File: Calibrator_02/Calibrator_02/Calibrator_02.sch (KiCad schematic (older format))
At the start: 22 parts, among them J1 Conn_01x04, J2 DB9_Female_MountingHoles, J3 Conn_Coaxial, J4 Conn_01x01_Female, J5 Conn_01x01_Female, J6 Conn_01x04, M1 AW9523BTQR, U1 KAQY214STLD, U2 KAQY214STLD, U3 KAQY214STLD, U4 KAQY214STLD, U5 KAQY214STLD, U6 KAQY214STLD, U7 KAQY214STLD, U8 KAQY214STLD

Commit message: Added Resistors to Diodes
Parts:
- added R10, R17: 95.3 1%, Resistor_SMD:R_0201_0603Metric_Pad0.64x0.40mm_HandSolder, symbol Device:R
- added R11, R12, R13, R14, R15, R16: 84.5 1%, Resistor_SMD:R_0201_0603Metric_Pad0.64x0.40mm_HandSolder, symbol Device:R
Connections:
- net +3V3: now also R10.1, R11.1, R12.1, R13.1, R14.2, R15.2, R16.2, R17.2; no longer D1.2 (A), D2.2 (A), U1.1 (A), U2.1 (A), U4.1 (A), U5.1 (A), U7.1 (A), U8.1 (A)
- new net: R13.2, U4.1 (A)
- new net: R15.1, U7.1 (A)
- new net: D1.2 (A), R10.2
- new net: D2.2 (A), R17.1
- new net: R14.1, U5.1 (A)
- new net: R12.2, U2.1 (A)
- new net: R16.1, U8.1 (A)
- new net: R11.2, U1.1 (A)
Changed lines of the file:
@@
 Wire Wire Line
 	2150 6600 2750 6600
-Wire Wire Line
-	7900 700  6550 700
-Connection ~ 6550 700
-Wire Wire Line
-	1700 700  3700 700
-Connection ~ 5100 700
-Wire Wire Line
-	5100 700  6550 700
-Connection ~ 3700 700
-Wire Wire Line
-	3700 700  5100 700
 $Comp
 L power:+3.3V #PWR01
@@
 	-1   0    0    1
 $EndComp
-Connection ~ 4500 5500
-Wire Wire Line
-	4500 5500 5950 5500
-Connection ~ 5950 5500
-Wire Wire Line
-	5950 5500 7300 5500
 $Comp
 L Connector_Generic:Conn_01x04 J1
@@
 	1    0    0    -1
 $EndComp
-Wire Wire Line
-	7300 4750 7300 5500
-Wire Wire Line
-	5950 4850 5950 5500
-Wire Wire Line
-	4500 4800 4500 5500
-Wire Wire Line
-	2100 5500 3100 5500
-Wire Wire Line
-	3100 5100 3100 5500
-Connection ~ 3100 5500
-Wire Wire Line
-	3100 5500 4500 5500
-Wire Wire Line
-	7900 700  7900 1500
-Wire Wire Line
-	6550 700  6550 1600
-Wire Wire Line
-	5100 700  5100 1700
-Wire Wire Line
-	3700 700  3700 1350
 $Comp
 L Connector:Conn_Coaxial J?
@@
 	-1   0    0    1
 $EndComp
+Wire Wire Line
+	2100 5500 3100 5500
+Wire Wire Line
+	1700 700  3700 700
+$Comp
+L Device:R R10
+U 1 1 6283AB55
+P 3700 1200
+F 0 "R10" H 3770 1246 50  0000 L CNN
+F 1 "95.3 1%" H 3770 1155 50  0000 L CNN
+F 2 "Resistor_SMD:R_0201_0603Metric_Pad0.64x0.40mm_HandSolder" V 3630 1200 50  0001 C CNN
+F 3 "~" H 3700 1200 50  0001 C CNN
+F 4 "C218188" H 3700 1200 50  0001 C CNN "LCSC"
+	1    3700 1200
+	1    0    0    -1
+$EndComp
+$Comp
+L Device:R R13
+U 1 1 6283B6FF
+P 5100 1550
+F 0 "R13" H 5170 1596 50  0000 L CNN
+F 1 "84.5 1%" H 5170 1505 50  0000 L CNN
+F 2 "Resistor_SMD:R_0201_0603Metric_Pad0.64x0.40mm_HandSolder" V 5030 1550 50  0001 C CNN
+F 3 "~" H 5100 1550 50  0001 C CNN
+F 4 "C177824" H 5100 1550 50  0001 C CNN "LCSC"
+	1    5100 1550
+	1    0    0    -1
+$EndComp
+$Comp
+L Device:R R17
+U 1 1 6283E3B1
+P 3100 5250
+F 0 "R17" H 3170 5296 50  0000 L CNN
+F 1 "95.3 1%" H 3170 5205 50  0000 L CNN
+F 2 "Resistor_SMD:R_0201_0603Metric_Pad0.64x0.40mm_HandSolder" V 3030 5250 50  0001 C CNN
+F 3 "~" H 3100 5250 50  0001 C CNN
+F 4 "C218188" H 3100 5250 50  0001 C CNN "LCSC"
+	1    3100 5250
+	1    0    0    -1
+$EndComp
+$Comp
+L Device:R R12
+U 1 1 6287964B
+P 6550 1450
+F 0 "R12" H 6620 1496 50  0000 L CNN
+F 1 "84.5 1%" H 6620 1405 50  0000 L CNN
+F 2 "Resistor_SMD:R_0201_0603Metric_Pad0.64x0.40mm_HandSolder" V 6480 1450 50  0001 C CNN
+F 3 "~" H 6550 1450 50  0001 C CNN
+F 4 "C177824" H 6550 1450 50  0001 C CNN "LCSC"
+	1    6550 1450
+	1    0    0    -1
+$EndComp
+$Comp
+L Device:R R11
+U 1 1 6287B511
+P 7900 1350
+F 0 "R11" H 7970 1396 50  0000 L CNN
+F 1 "84.5 1%" H 7970 1305 50  0000 L CNN
+F 2 "Resistor_SMD:R_0201_0603Metric_Pad0.64x0.40mm_HandSolder" V 7830 1350 50  0001 C CNN
+F 3 "~" H 7900 1350 50  0001 C CNN
+F 4 "C177824" H 7900 1350 50  0001 C CNN "LCSC"
+	1    7900 1350
+	1    0    0    -1
+$EndComp
+$Comp
+L Device:R R15
+U 1 1 6287D697
+P 4500 4950
+F 0 "R15" H 4570 4996 50  0000 L CNN
+F 1 "84.5 1%" H 4570 4905 50  0000 L CNN
+F 2 "Resistor_SMD:R_0201_0603Metric_Pad0.64x0.40mm_HandSolder" V 4430 4950 50  0001 C CNN
+F 3 "~" H 4500 4950 50  0001 C CNN
+F 4 "C177824" H 4500 4950 50  0001 C CNN "LCSC"
+	1    4500 4950
+	1    0    0    -1
+$EndComp
+$Comp
+L Device:R R16
+U 1 1 6287F5DB
+P 5950 5000
+F 0 "R16" H 6020 5046 50  0000 L CNN
+F 1 "84.5 1%" H 6020 4955 50  0000 L CNN
+F 2 "Resistor_SMD:R_0201_0603Metric_Pad0.64x0.40mm_HandSolder" V 5880 5000 50  0001 C CNN
+F 3 "~" H 5950 5000 50  0001 C CNN
+F 4 "C177824" H 5950 5000 50  0001 C CNN "LCSC"
+	1    5950 5000
+	1    0    0    -1
+$EndComp
+$Comp
+L Device:R R14
+U 1 1 628831ED
+P 7300 4900
+F 0 "R14" H 7370 4946 50  0000 L CNN
+F 1 "84.5 1%" H 7370 4855 50  0000 L CNN
+F 2 "Resistor_SMD:R_0201_0603Metric_Pad0.64x0.40mm_HandSolder" V 7230 4900 50  0001 C CNN
+F 3 "~" H 7300 4900 50  0001 C CNN
+F 4 "C177824" H 7300 4900 50  0001 C CNN "LCSC"
+	1    7300 4900
+	1    0    0    -1
+$EndComp
+Wire Wire Line
+	7300 5050 7300 5500
+Wire Wire Line
+	5950 5150 5950 5500
+Connection ~ 5950 5500
+Wire Wire Line
+	5950 5500 7300 5500
+Wire Wire Line
+	4500 5100 4500 5500
+Connection ~ 4500 5500
+Wire Wire Line
+	4500 5500 5950 5500
+Wire Wire Line
+	3100 5400 3100 5500
+Connection ~ 3100 5500
+Wire Wire Line
+	3100 5500 4500 5500
+Connection ~ 3700 700
+Wire Wire Line
+	3700 700  5100 700
+Wire Wire Line
+	5100 700  5100 1400
+Connection ~ 5100 700
+Wire Wire Line
+	5100 700  6550 700
+Wire Wire Line
+	6550 700  6550 1300
+Connection ~ 6550 700
+Wire Wire Line
+	6550 700  7900 700
+Wire Wire Line
+	7900 1200 7900 700
+Wire Wire Line
+	3700 700  3700 1050
 $EndSCHEMATC

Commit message: Update
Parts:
- removed JP1: Jumper, Jumper:SolderJumper-2_P1.3mm_Open_RoundedPad1.0x1.5mm, symbol Device:Jumper
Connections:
- net +3V3: now also J4.1 (Pin_1), M1.23 (RSTN)
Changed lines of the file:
@@
 Wire Wire Line
 	9050 2900 9350 2900
-Wire Wire Line
-	1700 6500 1800 6500
-$Comp
-L Device:Jumper JP1
-U 1 1 627E9ED5
-P 1800 6200
-F 0 "JP1" V 1754 6327 50  0000 L CNN
-F 1 "Jumper" V 1845 6327 50  0000 L CNN
-F 2 "Jumper:SolderJumper-2_P1.3mm_Open_RoundedPad1.0x1.5mm" H 1800 6200 50  0001 C CNN
-F 3 "~" H 1800 6200 50  0001 C CNN
-	1    1800 6200
-	0    1    1    0
-$EndComp
-Connection ~ 1800 6500
-Wire Wire Line
-	1800 6500 2750 6500
 $Comp
 L power:+3.3V #PWR09
@@
 Wire Wire Line
 	3700 700  3700 1050
+Wire Wire Line
+	1700 6500 1800 6500
+Wire Wire Line
+	1800 5900 1800 6500
+Connection ~ 1800 6500
+Wire Wire Line
+	1800 6500 2750 6500
 $EndSCHEMATC

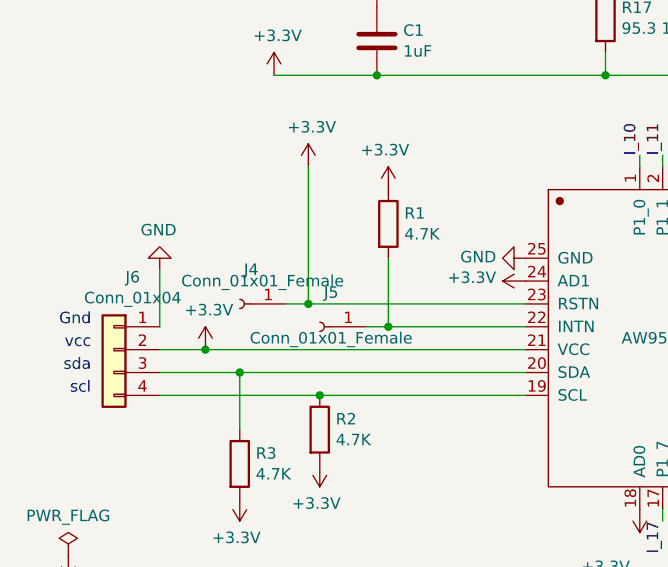
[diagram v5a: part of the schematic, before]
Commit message: Fixed footprint
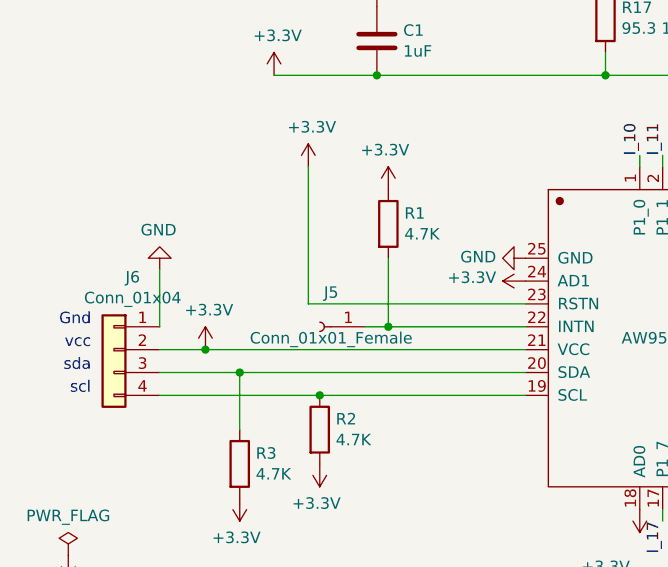
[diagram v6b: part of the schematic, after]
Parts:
- removed J4: Conn_01x01_Female, Connector_PinSocket_2.54mm:PinSocket_1x01_P2.54mm_Horizontal, symbol Connector:Conn_01x01_Female
- R10, R11, R12, R13, R14, R15, R16, R17: footprint Resistor_SMD:R_0201_0603Metric_Pad0.64x0.40mm_HandSolder -> Resistor_SMD:R_0603_1608Metric_Pad0.98x0.95mm_HandSolder
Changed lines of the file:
@@
-$EndComp
-$Comp
-L Connector:Conn_01x01_Female J4
-U 1 1 6281DACE
-P 1500 6500
-F 0 "J4" H 1450 6650 50  0000 C CNN
-F 1 "Conn_01x01_Female" H 1400 6600 50  0000 C CNN
-F 2 "Connector_PinSocket_2.54mm:PinSocket_1x01_P2.54mm_Horizontal" H 1500 6500 50  0001 C CNN
-F 3 "~" H 1500 6500 50  0001 C CNN
-	1    1500 6500
-	-1   0    0    -1
 $EndComp
 $Comp
@@
 F 0 "R10" H 3770 1246 50  0000 L CNN
 F 1 "95.3 1%" H 3770 1155 50  0000 L CNN
-F 2 "Resistor_SMD:R_0201_0603Metric_Pad0.64x0.40mm_HandSolder" V 3630 1200 50  0001 C CNN
+F 2 "Resistor_SMD:R_0603_1608Metric_Pad0.98x0.95mm_HandSolder" V 3630 1200 50  0001 C CNN
 F 3 "~" H 3700 1200 50  0001 C CNN
 F 4 "C218188" H 3700 1200 50  0001 C CNN "LCSC"
@@
 F 0 "R13" H 5170 1596 50  0000 L CNN
 F 1 "84.5 1%" H 5170 1505 50  0000 L CNN
-F 2 "Resistor_SMD:R_0201_0603Metric_Pad0.64x0.40mm_HandSolder" V 5030 1550 50  0001 C CNN
+F 2 "Resistor_SMD:R_0603_1608Metric_Pad0.98x0.95mm_HandSolder" V 5030 1550 50  0001 C CNN
 F 3 "~" H 5100 1550 50  0001 C CNN
 F 4 "C177824" H 5100 1550 50  0001 C CNN "LCSC"
@@
 F 0 "R17" H 3170 5296 50  0000 L CNN
 F 1 "95.3 1%" H 3170 5205 50  0000 L CNN
-F 2 "Resistor_SMD:R_0201_0603Metric_Pad0.64x0.40mm_HandSolder" V 3030 5250 50  0001 C CNN
+F 2 "Resistor_SMD:R_0603_1608Metric_Pad0.98x0.95mm_HandSolder" V 3030 5250 50  0001 C CNN
 F 3 "~" H 3100 5250 50  0001 C CNN
 F 4 "C218188" H 3100 5250 50  0001 C CNN "LCSC"
@@
 F 0 "R12" H 6620 1496 50  0000 L CNN
 F 1 "84.5 1%" H 6620 1405 50  0000 L CNN
-F 2 "Resistor_SMD:R_0201_0603Metric_Pad0.64x0.40mm_HandSolder" V 6480 1450 50  0001 C CNN
+F 2 "Resistor_SMD:R_0603_1608Metric_Pad0.98x0.95mm_HandSolder" V 6480 1450 50  0001 C CNN
 F 3 "~" H 6550 1450 50  0001 C CNN
 F 4 "C177824" H 6550 1450 50  0001 C CNN "LCSC"
@@
 F 0 "R11" H 7970 1396 50  0000 L CNN
 F 1 "84.5 1%" H 7970 1305 50  0000 L CNN
-F 2 "Resistor_SMD:R_0201_0603Metric_Pad0.64x0.40mm_HandSolder" V 7830 1350 50  0001 C CNN
+F 2 "Resistor_SMD:R_0603_1608Metric_Pad0.98x0.95mm_HandSolder" V 7830 1350 50  0001 C CNN
 F 3 "~" H 7900 1350 50  0001 C CNN
 F 4 "C177824" H 7900 1350 50  0001 C CNN "LCSC"
@@
 F 0 "R15" H 4570 4996 50  0000 L CNN
 F 1 "84.5 1%" H 4570 4905 50  0000 L CNN
-F 2 "Resistor_SMD:R_0201_0603Metric_Pad0.64x0.40mm_HandSolder" V 4430 4950 50  0001 C CNN
+F 2 "Resistor_SMD:R_0603_1608Metric_Pad0.98x0.95mm_HandSolder" V 4430 4950 50  0001 C CNN
 F 3 "~" H 4500 4950 50  0001 C CNN
 F 4 "C177824" H 4500 4950 50  0001 C CNN "LCSC"
@@
 F 0 "R16" H 6020 5046 50  0000 L CNN
 F 1 "84.5 1%" H 6020 4955 50  0000 L CNN
-F 2 "Resistor_SMD:R_0201_0603Metric_Pad0.64x0.40mm_HandSolder" V 5880 5000 50  0001 C CNN
+F 2 "Resistor_SMD:R_0603_1608Metric_Pad0.98x0.95mm_HandSolder" V 5880 5000 50  0001 C CNN
 F 3 "~" H 5950 5000 50  0001 C CNN
 F 4 "C177824" H 5950 5000 50  0001 C CNN "LCSC"
@@
 F 0 "R14" H 7370 4946 50  0000 L CNN
 F 1 "84.5 1%" H 7370 4855 50  0000 L CNN
-F 2 "Resistor_SMD:R_0201_0603Metric_Pad0.64x0.40mm_HandSolder" V 7230 4900 50  0001 C CNN
+F 2 "Resistor_SMD:R_0603_1608Metric_Pad0.98x0.95mm_HandSolder" V 7230 4900 50  0001 C CNN
 F 3 "~" H 7300 4900 50  0001 C CNN
 F 4 "C177824" H 7300 4900 50  0001 C CNN "LCSC"
@@
 	3700 700  3700 1050
 Wire Wire Line
-	1700 6500 1800 6500
-Wire Wire Line
 	1800 5900 1800 6500
-Connection ~ 1800 6500
 Wire Wire Line
 	1800 6500 2750 6500
